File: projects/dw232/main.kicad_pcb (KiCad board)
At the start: 4 copper layers, 27 parts, among them P101 CONN_01X07, Q501 MMBT3904, Q502 MMBT3904, U501 LM741, U502 LM741, U503 2DW232

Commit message: remove old gerbers
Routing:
- net REF: track 0.00 -> 95.4 mm, vias 0 -> 1
- net H-GND: track 0.00 -> 84.8 mm, vias 0 -> 1
- net Net-(Q501-Pad2): track 0.00 -> 70.9 mm
- net Net-(R503-Pad2): track 0.00 -> 63.4 mm
- net Net-(Q502-Pad2): track 0.00 -> 36.7 mm
- net AGND: track 0.00 -> 34.7 mm, vias 0 -> 2
- net Net-(C502-Pad1): track 0.00 -> 34.1 mm
- net +VE: track 0.00 -> 31.7 mm, vias 0 -> 4
- net Net-(R509-Pad2): track 0.00 -> 29.7 mm, vias 0 -> 1
- net Net-(C501-Pad2): track 0.00 -> 21.4 mm
- net Net-(R502-Pad1): track 0.00 -> 18.5 mm, vias 0 -> 2
- net -VE: track 0.00 -> 12.1 mm, vias 0 -> 5
- net Net-(C501-Pad1): track 0.00 -> 5.76 mm
- net Net-(Q502-Pad1): track 0.00 -> 5.50 mm
- net Net-(R508-Pad1): track 0.00 -> 4.00 mm
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
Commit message: update
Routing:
- net +VE: track 31.7 -> 28.7 mm, vias 4 -> 3
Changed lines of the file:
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@@
     (thickness 1.6)
     (drawings 0)
-    (tracks 169)
+    (tracks 167)
     (zones 0)
     (modules 27)
@@
     (visible_elements FFFFEF7F)
     (pcbplotparams
-      (layerselection 0x2bfaa_80000007)
+      (layerselection 0x012a0_80000007)
       (usegerberextensions false)
       (excludeedgelayer true)
@@
       (drillshape 0)
       (scaleselection 1)
-      (outputdirectory ../gerber))
+      (outputdirectory gerber/))
   )
   (net 0 "")
@@
       (net 11 "Net-(R508-Pad1)"))
   )
-  (segment (start 54 46.5) (end 52.5 46.5) (width 0.75) (layer F.Cu) (net 1) (status 400000))
+  (segment (start 54 46.5) (end 52.5 46.5) (width 0.75) (layer F.Cu) (net 1))
   (via (at 52 46) (size 1) (drill 0.5) (layers F.Cu B.Cu) (net 1))
   (segment (start 52.5 46.5) (end 52 46) (width 0.75) (layer F.Cu) (net 1))
@@
   (segment (start 68.00178 36.99822) (end 68 37) (width 0.75) (layer F.Cu) (net 1))
   (via (at 68 37) (size 1) (drill 0.5) (layers F.Cu B.Cu) (net 1))
-  (segment (start 68.00178 36.99822) (end 68.00178 34) (width 0.75) (layer F.Cu) (net 1) (status 800000))
+  (segment (start 68.00178 36.99822) (end 68.00178 34) (width 0.75) (layer F.Cu) (net 1))
   (segment (start 68.365 37.365) (end 68 37) (width 0.75) (layer F.Cu) (net 1))
-  (segment (start 55 33.5) (end 55 31) (width 0.75) (layer F.Cu) (net 1) (status 400000))
+  (segment (start 55 33.5) (end 55 31) (width 0.75) (layer F.Cu) (net 1))
   (via (at 55 31) (size 1) (drill 0.5) (layers F.Cu B.Cu) (net 1))
-  (segment (start 45 34) (end 48 34) (width 0.75) (layer F.Cu) (net 1) (status 400000))
-  (via (at 48 34) (size 1) (drill 0.5) (layers F.Cu B.Cu) (net 1))
   (segment (start 65.875 41.825) (end 68.365 41.825) (width 0.75) (layer F.Cu) (net 1))
   (segment (start 65.55 41.5) (end 65.875 41.825) (width 0.75) (layer F.Cu) (net 1))
   (segment (start 64 41.5) (end 65.55 41.5) (width 0.75) (layer F.Cu) (net 1))
-  (segment (start 68.365 40.3) (end 68.365 41) (width 0.75) (layer F.Cu) (net 1) (status 800000))
-  (segment (start 68.365 41) (end 68.365 41.825) (width 0.75) (layer F.Cu) (net 1) (status 400000))
+  (segment (start 68.365 40.3) (end 68.365 41) (width 0.75) (layer F.Cu) (net 1))
+  (segment (start 68.365 41) (end 68.365 41.825) (width 0.75) (layer F.Cu) (net 1))
   (segment (start 54 46.5) (end 54 47.75) (width 0.75) (layer F.Cu) (net 1))
   (segment (start 56.8517 33.8017) (end 56.55 33.5) (width 0.75) (layer F.Cu) (net 1))
@@
   (segment (start 57.44 47.75) (end 54 47.75) (width 0.75) (layer F.Cu) (net 1))
   (segment (start 58.365 46.825) (end 57.44 47.75) (width 0.75) (layer F.Cu) (net 1))
-  (segment (start 64 49.5) (end 64 52) (width 0.75) (layer F.Cu) (net 2) (status 400000))
+  (segment (start 64 49.5) (end 64 52) (width 0.75) (layer F.Cu) (net 2))
   (via (at 64 52) (size 1) (drill 0.5) (layers F.Cu B.Cu) (net 2))
   (via (at 71.558 44.175) (size 1) (layers F.Cu B.Cu) (net 2))
@@
   (segment (start 65.6 35.55) (end 65.6 34.6702) (width 0.75) (layer F.Cu) (net 14))
   (segment (start 64 35.55) (end 65.6 35.55) (width 0.75) (layer F.Cu) (net 14))
-  (segment (start 74 41.5) (end 74 39) (width 0.75) (layer F.Cu) (net 15) (status 400000))
+  (segment (start 74 41.5) (end 74 39) (width 0.75) (layer F.Cu) (net 15))
   (via (at 74 39) (size 1) (drill 0.5) (layers F.Cu B.Cu) (net 15))
   (segment (start 67.5 49) (end 67.5 50.5) (width 0.75) (layer F.Cu) (net 15))

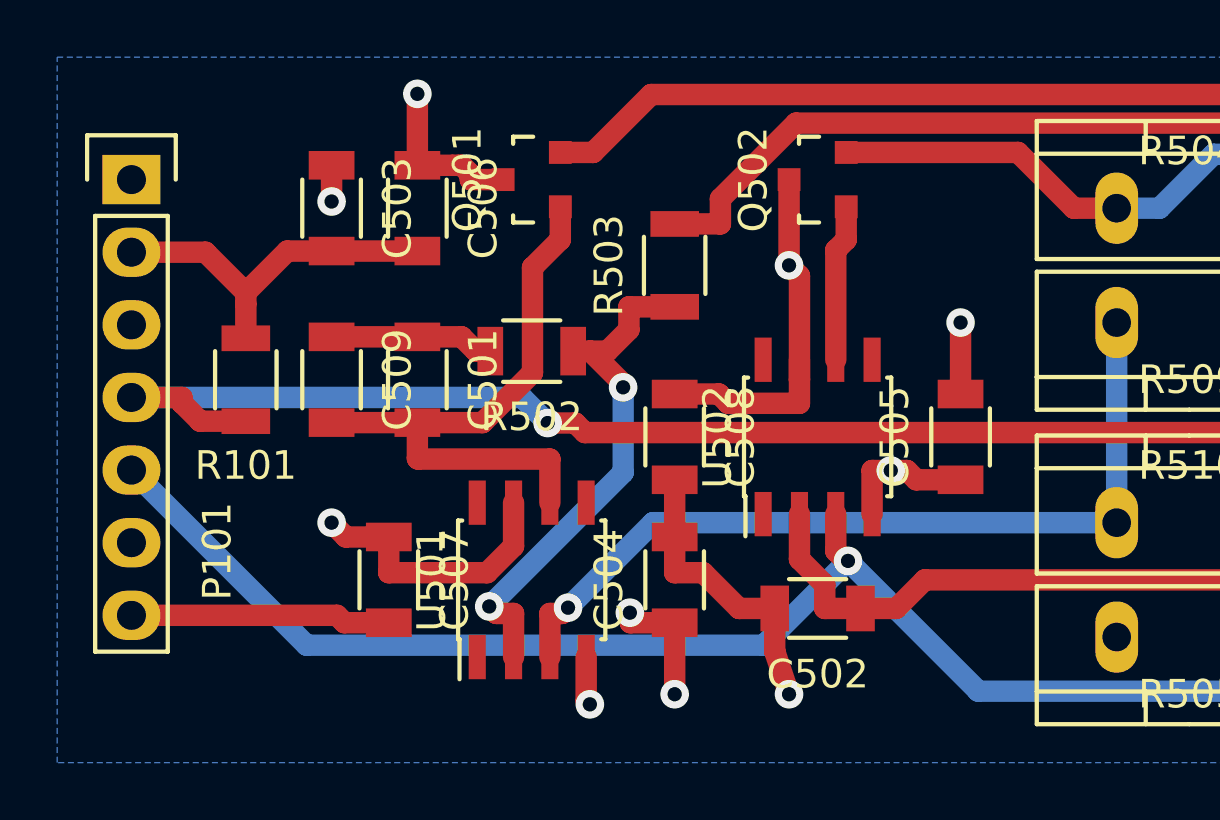
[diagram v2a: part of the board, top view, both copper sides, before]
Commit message: reposition silkscreen lttering
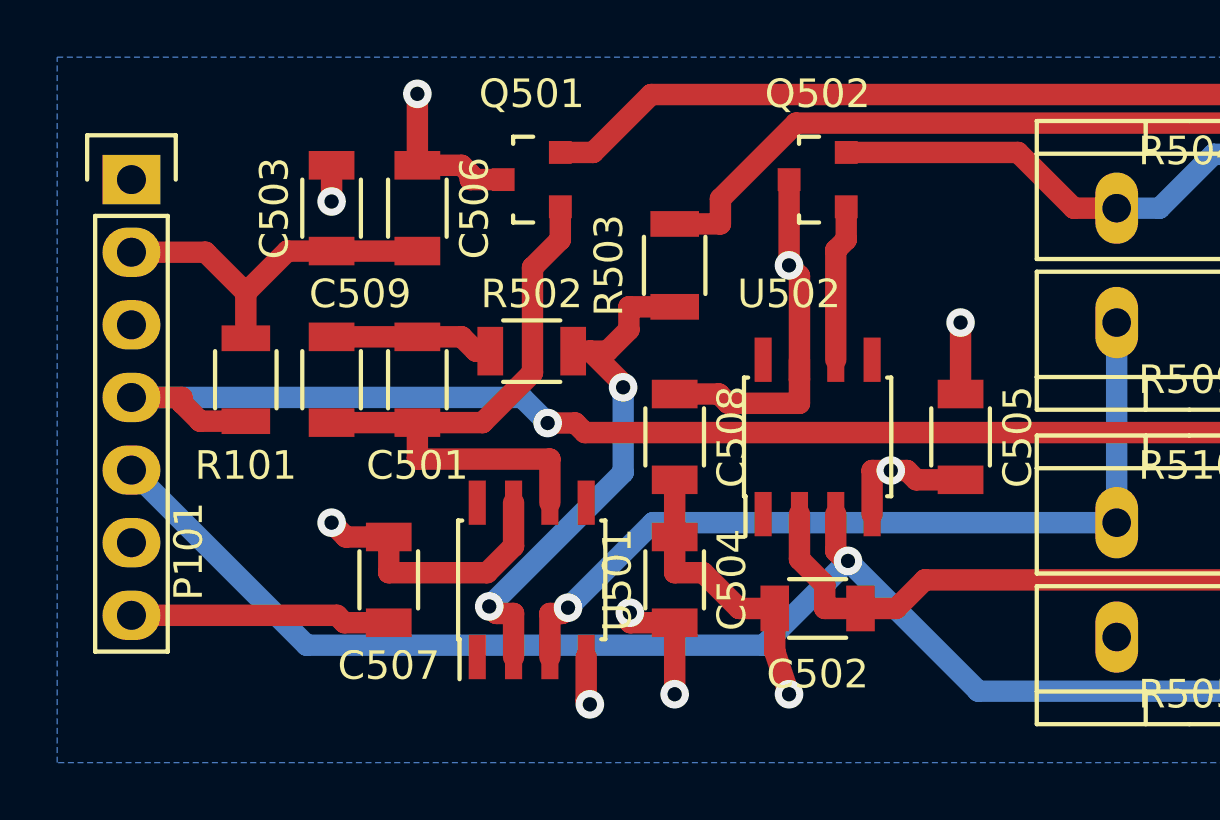
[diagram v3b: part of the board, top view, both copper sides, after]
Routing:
- removed copper zone on In1.Cu, net AGND

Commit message: fix front and back silk
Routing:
- added copper zone on In1.Cu, net AGND
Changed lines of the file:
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@@
   (general
     (links 52)
-    (no_connects 7)
-    (area 42 29 138.684001 54.394001)
+    (no_connects 0)
+    (area 42 29 139.000001 54.000001)
     (thickness 1.6)
     (drawings 0)
@@
   (layers
     (0 F.Cu signal)
-    (1 In1.Cu signal)
+    (1 In1.Cu signal hide)
     (2 In2.Cu signal hide)
     (31 B.Cu signal hide)
@@
     (36 B.SilkS user hide)
     (37 F.SilkS user hide)
-    (38 B.Mask user hide)
+    (38 B.Mask user)
     (39 F.Mask user hide)
-    (40 Dwgs.User user)
+    (40 Dwgs.User user hide)
     (41 Cmts.User user)
     (42 Eco1.User user)
@@
   (segment (start 63.2433 46) (end 60.27 48.9733) (width 0.75) (layer B.Cu) (net 18))
   (segment (start 79.46 46) (end 63.2433 46) (width 0.75) (layer B.Cu) (net 18) (status 10))
+  (zone (net 0) (net_name "") (layer F.Mask) (hatch edge 0.508)
+    (connect_pads (clearance 0.508))
+    (min_thickness 0.254)
+    (fill yes (arc_segments 16) (thermal_gap 0.508) (thermal_bridge_width 0.508))
+    (polygon
+      (pts
+        (xy 139 54) (xy 42 54) (xy 42 29) (xy 139 29)
+      )
+    )
+  )
+  (zone (net 15) (net_name AGND) (layer In1.Cu) (hatch edge 0.508)
+    (connect_pads (clearance 0.508))
+    (min_thickness 0.254)
+    (fill yes (arc_segments 16) (thermal_gap 0.508) (thermal_bridge_width 0.508))
+    (polygon
+      (pts
+        (xy 139 54) (xy 42 54) (xy 42 29) (xy 139 29)
+      )
+    )
+  )
   (zone (net 1) (net_name +VE) (layer In2.Cu) (hatch edge 0.508)
     (connect_pads (clearance 0.508))
@@
     (polygon
       (pts
-        (xy 138.684 54.394) (xy 42.402 54.394) (xy 42.402 29.718) (xy 138.684 29.718)
+        (xy 139 54) (xy 42 54) (xy 42 29) (xy 139 29)
       )
     )
@@
     (polygon
       (pts
-        (xy 138.684 54.394) (xy 42.402 54.394) (xy 42.402 29.718) (xy 138.684 29.718)
+        (xy 139 54) (xy 42 54) (xy 42 29) (xy 139 29)
       )
     )
   )
-  (zone (net 0) (net_name "") (layer F.Mask) (hatch edge 0.508)
+  (zone (net 0) (net_name "") (layer B.Mask) (hatch edge 0.508)
     (connect_pads (clearance 0.508))
     (min_thickness 0.254)
@@
     (polygon
       (pts
-        (xy 129 54) (xy 42 54) (xy 42 29) (xy 129 29)
+        (xy 139 54) (xy 42 54) (xy 42 29) (xy 139 29)
       )
     )

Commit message: fix fills, text
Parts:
- moved P101 2.00 mm to (43.0, 34.0)
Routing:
- net H-GND: track 84.8 -> 88.8 mm
- net AGND: track 34.7 -> 38.7 mm
- net REF: track 95.4 -> 96.9 mm
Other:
- board text added: "+VE"
- board text added: "-VE"
- board text added: "AGND"
- board text added: "HGND"
- board text added: "REF"
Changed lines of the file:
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@@
     (links 52)
     (no_connects 0)
-    (area 42 29 139.000001 54.000001)
+    (area 40 29 139.000001 54.000001)
     (thickness 1.6)
-    (drawings 0)
+    (drawings 7)
     (tracks 164)
     (zones 0)
@@
     (1 In1.Cu signal hide)
     (2 In2.Cu signal hide)
-    (31 B.Cu signal hide)
+    (31 B.Cu signal)
     (33 F.Adhes user hide)
     (35 F.Paste user hide)
@@
     (pad_to_mask_clearance 0)
     (aux_axis_origin 0 0)
-    (grid_origin 63 33)
+    (grid_origin 28 21)
     (visible_elements FFFFFF7F)
     (pcbplotparams
@@
   )
   (module Pin_Headers:Pin_Header_Straight_1x07 (layer F.Cu)
-    (at 45 34)
+    (at 43 34)
     (descr "Through hole pin header")
     (tags "pin header")
-    (fp_text reference P101 (at 2 13 90) (layer F.SilkS)
+    (fp_text reference P101 (at 1 -3 180) (layer F.SilkS)
       (effects (font (size 1 1) (thickness 0.15)))
     )
@@
     (pad 2 thru_hole oval (at 2.54 0 90) (size 2.49936 1.50114) (drill 1.00076) (layers *.Cu *.Mask F.SilkS)
       (net 11 "Net-(R508-Pad1)"))
+  )
+  (gr_text "AGND\n" (at 44.8 49.2) (layer F.SilkS)
+    (effects (font (size 1.5 1) (thickness 0.25)) (justify left))
+  )
+  (gr_text "AGND\n" (at 44.8 46.8) (layer F.SilkS)
+    (effects (font (size 1.5 1) (thickness 0.25)) (justify left))
+  )
+  (gr_text "REF\n" (at 44.8 44.4) (layer F.SilkS)
+    (effects (font (size 1.5 1) (thickness 0.25)) (justify left))
+  )
+  (gr_text "HGND\n" (at 44.8 41.6) (layer F.SilkS)
+    (effects (font (size 1.5 1) (thickness 0.25)) (justify left))
+  )
+  (gr_text "-VE\n" (at 44.8 39.2) (layer F.SilkS)
+    (effects (font (size 1.5 1) (thickness 0.25)) (justify left))
+  )
+  (gr_text AGND (at 45 36.6) (layer F.SilkS)
+    (effects (font (size 1.5 1) (thickness 0.25)) (justify left))
+  )
+  (gr_text +VE (at 44.8 33.8) (layer F.SilkS)
+    (effects (font (size 1.5 1) (thickness 0.25)) (justify left))
   )
   (segment (start 54 46.5) (end 52.5 46.5) (width 0.75) (layer F.Cu) (net 1) (status 10))
@@
   (segment (start 67.1147 50.2853) (end 70.0625 47.3375) (width 0.75) (layer B.Cu) (net 3))
   (segment (start 51.1253 50.2853) (end 67.1147 50.2853) (width 0.75) (layer B.Cu) (net 3))
-  (segment (start 45 44.16) (end 51.1253 50.2853) (width 0.75) (layer B.Cu) (net 3) (status 10))
+  (segment (start 43 44.16) (end 51.1253 50.2853) (width 0.75) (layer B.Cu) (net 3) (status 10))
   (segment (start 57.05 40) (end 56.55 39.5) (width 0.75) (layer F.Cu) (net 4))
   (segment (start 57.55 40) (end 57.05 40) (width 0.75) (layer F.Cu) (net 4) (status 10))
@@
   (segment (start 67.5 50.5) (end 68 52) (width 0.75) (layer F.Cu) (net 15))
   (segment (start 52.19 49.24) (end 52.45 49.5) (width 0.75) (layer F.Cu) (net 15))
-  (segment (start 45 49.24) (end 52.19 49.24) (width 0.75) (layer F.Cu) (net 15) (status 10))
+  (segment (start 43 49.24) (end 52.19 49.24) (width 0.75) (layer F.Cu) (net 15) (status 10))
   (segment (start 54 49.5) (end 52.45 49.5) (width 0.75) (layer F.Cu) (net 15) (status 10))
   (segment (start 52 36.5) (end 55 36.5) (width 0.75) (layer F.Cu) (net 15) (status 30))
@@
   (segment (start 49 39.55) (end 49 37.95) (width 0.75) (layer F.Cu) (net 15) (status 10))
   (segment (start 47.59 36.54) (end 49 37.95) (width 0.75) (layer F.Cu) (net 15))
-  (segment (start 45 36.54) (end 47.59 36.54) (width 0.75) (layer F.Cu) (net 15) (status 10))
+  (segment (start 43 36.54) (end 47.59 36.54) (width 0.75) (layer F.Cu) (net 15) (status 10))
   (segment (start 50.45 36.5) (end 49 37.95) (width 0.75) (layer F.Cu) (net 15))
   (via (at 59.5574 42.5141) (size 1) (layers F.Cu B.Cu) (net 16))
@@
   (segment (start 46.766 41.62) (end 46.766 41.816) (width 0.75) (layer F.Cu) (net 16))
   (segment (start 49 42.45) (end 47.4 42.45) (width 0.75) (layer F.Cu) (net 16) (status 10))
-  (segment (start 45 41.62) (end 46.766 41.62) (width 0.75) (layer F.Cu) (net 16) (status 10))
+  (segment (start 43 41.62) (end 46.766 41.62) (width 0.75) (layer F.Cu) (net 16) (status 10))
   (segment (start 58.6633 41.62) (end 59.5574 42.5141) (width 0.75) (layer B.Cu) (net 16))
-  (segment (start 45 41.62) (end 58.6633 41.62) (width 0.75) (layer B.Cu) (net 16) (status 10))
+  (segment (start 43 41.62) (end 58.6633 41.62) (width 0.75) (layer B.Cu) (net 16) (status 10))
   (segment (start 121.0668 44.794) (end 124 44.794) (width 0.75) (layer F.Cu) (net 16) (status 20))
   (segment (start 119.1215 42.8487) (end 121.0668 44.794) (width 0.75) (layer F.Cu) (net 16))
@@
     (polygon
       (pts
-        (xy 139 54) (xy 42 54) (xy 42 29) (xy 139 29)
+        (xy 139 54) (xy 40 54) (xy 40 29) (xy 139 29)
       )
     )
@@
     (polygon
       (pts
-        (xy 139 54) (xy 42 54) (xy 42 29) (xy 139 29)
+        (xy 139 54) (xy 40 54) (xy 40 29) (xy 139 29)
       )
     )
@@
     (polygon
       (pts
-        (xy 139 54) (xy 42 54) (xy 42 29) (xy 139 29)
+        (xy 139 54) (xy 40 54) (xy 40 29) (xy 139 29)
       )
     )
@@
     (polygon
       (pts
-        (xy 139 54) (xy 42 54) (xy 42 29) (xy 139 29)
+        (xy 139 54) (xy 40 54) (xy 40 29) (xy 139 29)
       )
     )
@@
     (polygon
       (pts
-        (xy 139 54) (xy 42 54) (xy 42 29) (xy 139 29)
+        (xy 139 54) (xy 40 54) (xy 40 29) (xy 139 29)
       )
     )

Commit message: copyright
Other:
- board text added: "Ver. 0.1 (C) JA, 2017 GNU"
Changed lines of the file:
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@@
     (area 40 29 139.000001 54.000001)
     (thickness 1.6)
-    (drawings 7)
+    (drawings 8)
     (tracks 164)
     (zones 0)
@@
     (1 In1.Cu signal hide)
     (2 In2.Cu signal hide)
-    (31 B.Cu signal)
+    (31 B.Cu signal hide)
     (33 F.Adhes user hide)
     (35 F.Paste user hide)
     (36 B.SilkS user hide)
-    (37 F.SilkS user hide)
-    (38 B.Mask user)
+    (37 F.SilkS user)
+    (38 B.Mask user hide)
     (39 F.Mask user hide)
     (40 Dwgs.User user hide)
@@
       (net 11 "Net-(R508-Pad1)"))
   )
+  (gr_text "Ver. 0.1 (C) JA, 2017\nGNU" (at 109 51) (layer F.SilkS)
+    (effects (font (size 1.5 1) (thickness 0.25)))
+  )
   (gr_text "AGND\n" (at 44.8 49.2) (layer F.SilkS)
